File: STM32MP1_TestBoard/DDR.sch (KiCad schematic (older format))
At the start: 63 parts, among them U1 STM32MP157xAB, U2 MT41K256M16TW-107

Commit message: updated bom, readme
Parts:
- removed U1: STM32MP157xAB, STM32MP151_LFBGA:BGA-361_19x19_16.0x16.0mm, symbol STM32MP151:STM32MP151xAB
- added U1: STM32MP157xAB, STM32MP151_LFBGA:BGA-361_19x19_16.0x16.0mm, symbol STM32MP15x:STM32MP157xAB
- gave numbers to parts that had none: 55

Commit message: minor schema updates
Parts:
- added R2, R52: 1K, Resistor_SMD:R_0402_1005Metric_Pad0.72x0.64mm_HandSolder, symbol Device:R
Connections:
- wire segments 311 -> 316
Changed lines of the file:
@@
 Wire Wire Line
 	4700 5175 5325 5175
-Text HLabel 5325 5175 2    50   Input ~ 0
-DDR_VREF
 Wire Wire Line
 	1500 8650 1500 8500
@@
 	1    0    0    -1
 $EndComp
+$Comp
+L Device:R R?
+U 1 1 5FDCF44A
+P 6150 8325
+AR Path="/5FBD70AB/5FDCF44A" Ref="R?"  Part="1"
+AR Path="/60386EBB/5FDCF44A" Ref="R2"  Part="1"
+F 0 "R2" H 6220 8371 50  0000 L CNN
+F 1 "1K" H 6220 8280 50  0000 L CNN
+F 2 "Resistor_SMD:R_0402_1005Metric_Pad0.72x0.64mm_HandSolder" V 6080 8325 50  0001 C CNN
+F 3 "~" H 6150 8325 50  0001 C CNN
+F 4 "~" H 6150 8325 50  0001 C CNN "Mfr"
+F 5 "~" H 6150 8325 50  0001 C CNN "PartNo"
+	1    6150 8325
+	1    0    0    -1
+$EndComp
+$Comp
+L Device:R R?
+U 1 1 5FDCF452
+P 6150 8900
+AR Path="/5FBD70AB/5FDCF452" Ref="R?"  Part="1"
+AR Path="/60386EBB/5FDCF452" Ref="R52"  Part="1"
+F 0 "R52" H 6220 8946 50  0000 L CNN
+F 1 "1K" H 6220 8855 50  0000 L CNN
+F 2 "Resistor_SMD:R_0402_1005Metric_Pad0.72x0.64mm_HandSolder" V 6080 8900 50  0001 C CNN
+F 3 "~" H 6150 8900 50  0001 C CNN
+F 4 "~" H 6150 8900 50  0001 C CNN "Mfr"
+F 5 "~" H 6150 8900 50  0001 C CNN "PartNo"
+	1    6150 8900
+	1    0    0    -1
+$EndComp
+Wire Wire Line
+	6975 8625 6150 8625
+Wire Wire Line
+	6150 8475 6150 8625
+Connection ~ 6150 8625
+Wire Wire Line
+	6150 8625 6150 8750
+$Comp
+L power:+1V35 #PWR?
+U 1 1 5FDCF45C
+P 6150 8075
+AR Path="/5FDCF45C" Ref="#PWR?"  Part="1"
+AR Path="/6044C48A/5FDCF45C" Ref="#PWR?"  Part="1"
+AR Path="/5FBD70AB/5FDCF45C" Ref="#PWR?"  Part="1"
+AR Path="/60386EBB/5FDCF45C" Ref="#PWR0127"  Part="1"
+F 0 "#PWR0127" H 6150 7925 50  0001 C CNN
+F 1 "+1V35" H 6165 8248 50  0000 C CNN
+F 2 "" H 6150 8075 50  0001 C CNN
+F 3 "" H 6150 8075 50  0001 C CNN
+	1    6150 8075
+	1    0    0    -1
+$EndComp
+Wire Wire Line
+	6150 8075 6150 8175
+$Comp
+L power:GNDS #PWR?
+U 1 1 5FDCF463
+P 6150 9150
+AR Path="/5FBD70AB/5FDCF463" Ref="#PWR?"  Part="1"
+AR Path="/60386EBB/5FDCF463" Ref="#PWR0134"  Part="1"
+F 0 "#PWR0134" H 6150 8900 50  0001 C CNN
+F 1 "GNDS" H 6155 8977 50  0000 C CNN
+F 2 "" H 6150 9150 50  0001 C CNN
+F 3 "" H 6150 9150 50  0001 C CNN
+	1    6150 9150
+	1    0    0    -1
+$EndComp
+Wire Wire Line
+	6150 9150 6150 9050
+Text Label 5325 5175 2    50   ~ 0
+DDR_VREF
+Text Label 6975 8625 2    50   ~ 0
+DDR_VREF
 $EndSCHEMATC

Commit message: updated schematic design
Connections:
- net labels added: 1.35V_VDDQ_DDR
- net labels removed: +1V35
- wire segments 316 -> 317
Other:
- moved on the sheet: C40, C41, C42, C43, C44, C45, C46, C47, C48, C49, C50, C51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

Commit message: layout update
backup. work in progress
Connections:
- net DDR_CLKN renamed DDR_CLK_N
- net DDR_CLKP renamed DDR_CLK_P
- net DDR_DQS0N renamed DDR_DQS0_N
- net DDR_DQS0P renamed DDR_DQS0_P
- net DDR_DQS1N renamed DDR_DQS1_N
- net DDR_DQS1P renamed DDR_DQS1_P
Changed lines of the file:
@@
 	8375 5125 9350 5125
 Text Label 1950 3325 0    50   ~ 0
-DDR_DQS0P
+DDR_DQS0_P
 Text Label 9350 5025 2    50   ~ 0
-DDR_DQS0P
+DDR_DQS0_P
 Text Label 9350 5125 2    50   ~ 0
-DDR_DQS0N
+DDR_DQS0_N
 Text Label 1950 3425 0    50   ~ 0
-DDR_DQS0N
+DDR_DQS0_N
 Wire Wire Line
 	1950 4625 2900 4625
@@
 	1950 5575 2900 5575
 Text Label 1950 4525 0    50   ~ 0
-DDR_DQS1P
+DDR_DQS1_P
 Text Label 1950 4625 0    50   ~ 0
-DDR_DQS1N
+DDR_DQS1_N
 Text Label 9350 4825 2    50   ~ 0
-DDR_DQS1P
+DDR_DQS1_P
 Text Label 9350 4925 2    50   ~ 0
-DDR_DQS1N
+DDR_DQS1_N
 Text Label 1950 3525 0    50   ~ 0
 DDR_DQM0
@@
 Wire Wire Line
 	6975 5025 6350 5025
-Text Label 6350 4825 0    50   ~ 0
-DDR_CLKP
-Text Label 6350 4925 0    50   ~ 0
-DDR_CLKN
 Text Label 6350 5025 0    50   ~ 0
 DDR_CKE
@@
 	4700 2625 5325 2625
 Text Label 5325 2525 2    50   ~ 0
-DDR_CLKP
+DDR_CLK_P
 Text Label 5325 2625 2    50   ~ 0
-DDR_CLKN
+DDR_CLK_N
 Wire Wire Line
 	8375 5325 8750 5325
@@
 	4450 8050 3825 8050
 Text Label 5375 8050 2    50   ~ 0
-DDR_CLKP
+DDR_CLK_P
 Text Label 3825 8050 0    50   ~ 0
-DDR_CLKN
+DDR_CLK_N
 $Comp
 L Device:R R14
@@
 Wire Wire Line
 	5075 9550 5275 9550
+Text Label 6350 4925 0    50   ~ 0
+DDR_CLK_N
+Text Label 6350 4825 0    50   ~ 0
+DDR_CLK_P
 $EndSCHEMATC

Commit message: updated to use stm32MP15x symbol library
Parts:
- U1: Mfr STMicroelectronics -> (none); PartNo STM32MP157FAB -> (none)
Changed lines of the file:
@@
 0.5 × VDD
-$Comp
-L STM32MP15x:STM32MP157xAB U1
-U 3 1 601FCD98
-P 3800 4125
-F 0 "U1" H 3800 5990 50  0000 C CNN
-F 1 "STM32MP157xAB" H 3800 5899 50  0000 C CNN
-F 2 "STM32MP151_LFBGA:BGA-361_19x19_16.0x16.0mm" H 3650 6025 50  0001 C CNN
-F 3 "https://www.st.com/resource/en/datasheet/stm32mp157f.pdf" H 4100 4625 50  0001 C CNN
-F 4 "STMicroelectronics" H 3800 4125 50  0001 C CNN "Mfr"
-F 5 "STM32MP157FAB" H 3800 4125 50  0001 C CNN "PartNo"
-	3    3800 4125
-	1    0    0    -1
-$EndComp
 $Comp
 L Device:R R?
@@
 Text Label 6350 4825 0    50   ~ 0
 DDR_CLK_P
+$Comp
+L STM32MP15x:STM32MP157xAB U1
+U 3 1 5FBF8FCC
+P 3800 4125
+F 0 "U1" H 3800 5990 50  0000 C CNN
+F 1 "STM32MP157xAB" H 3800 5899 50  0000 C CNN
+F 2 "STM32MP151_LFBGA:BGA-361_19x19_16.0x16.0mm" H 3650 6025 50  0001 C CNN
+F 3 "https://www.st.com/resource/en/datasheet/stm32mp151c.pdf" H 4450 4275 50  0001 C CNN
+	3    3800 4125
+	1    0    0    -1
+$EndComp
 $EndSCHEMATC

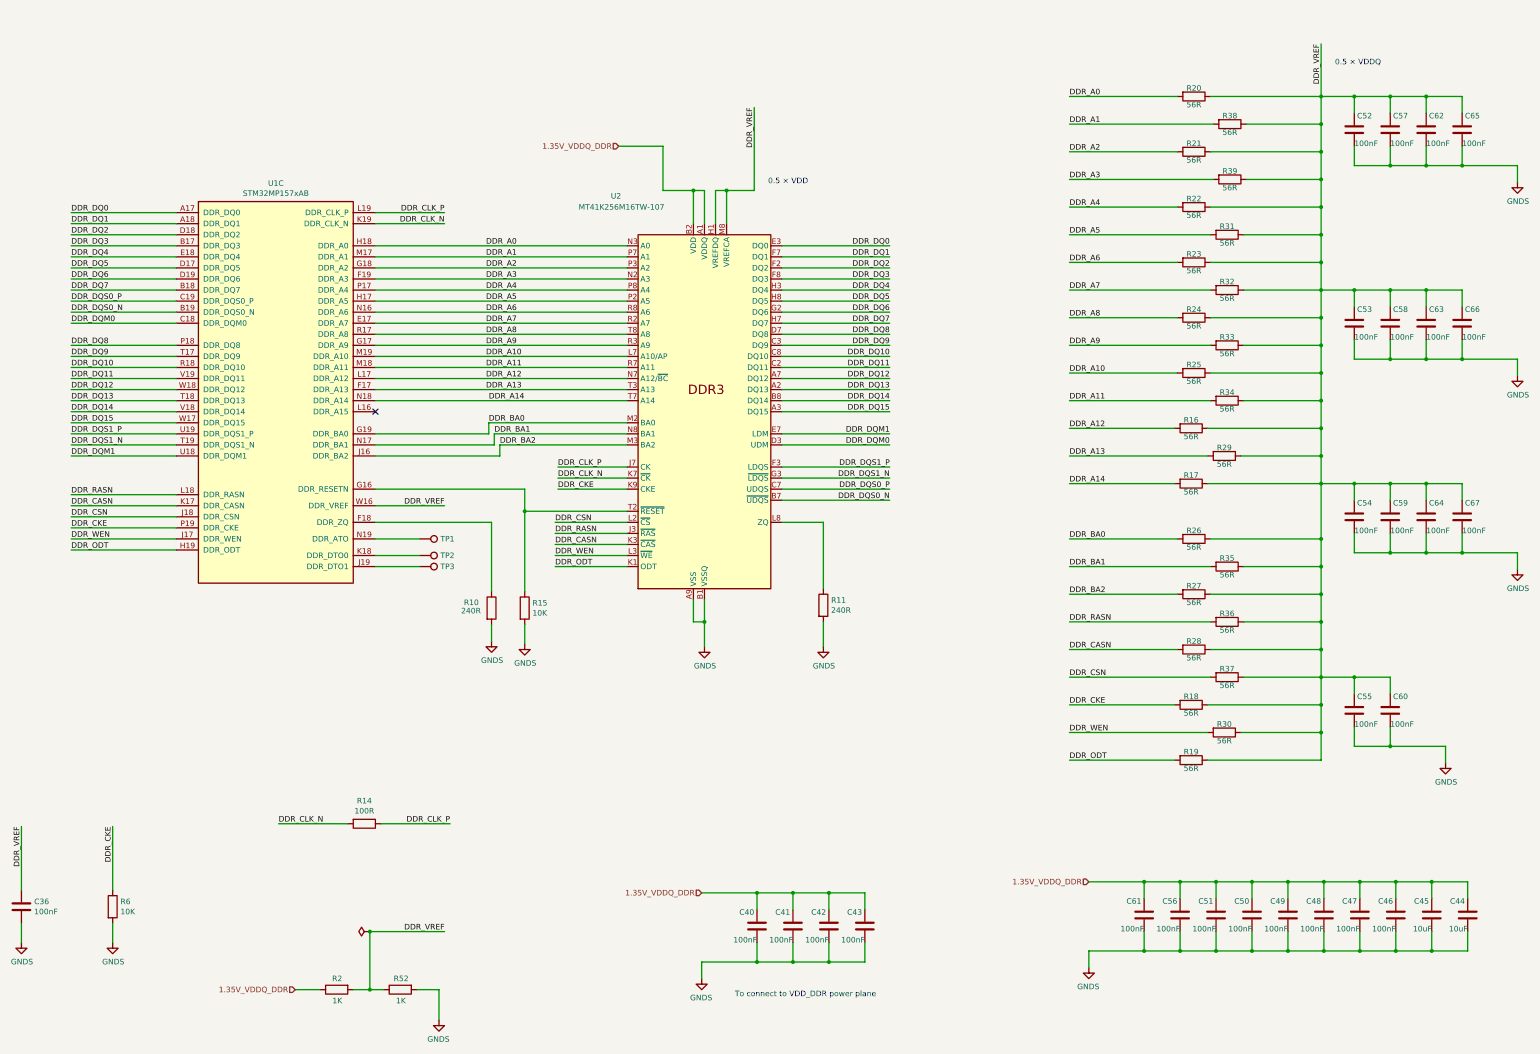
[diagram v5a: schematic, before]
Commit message: added traces for sdio, dsi and swd connectors
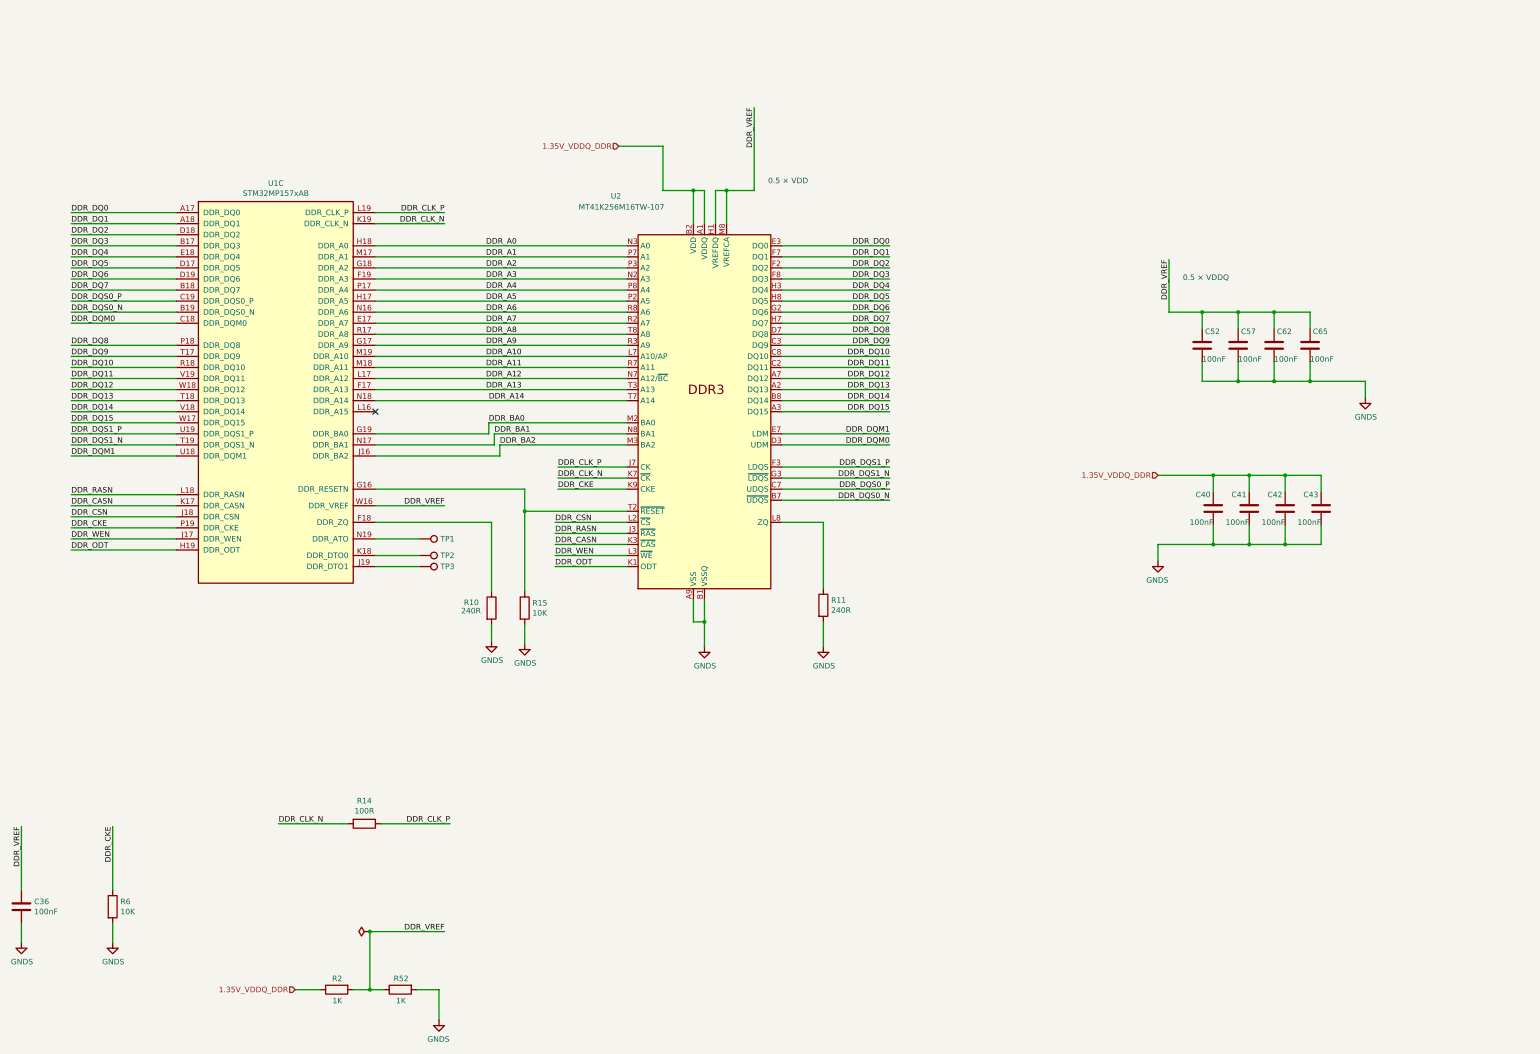
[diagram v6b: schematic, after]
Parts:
- removed C44, C45: 10uF, Capacitor_SMD:C_0402_1005Metric_Pad0.74x0.62mm_HandSolder, symbol Device:C
- removed C46, C47, C48, C49, C50, C51, C53, C54, C55, C56, C58, C59, C60, C61, C63, C64, C66, C67: 100nF, Capacitor_SMD:C_0402_1005Metric_Pad0.74x0.62mm_HandSolder, symbol Device:C
- removed R16, R17, R18, R19, R20, R21, R22, R23, R24, R25, R26, R27, R28, R29, R30, R31, R32, R33, R34, R35, R36, R37, R38, R39: 56R, Resistor_SMD:R_0402_1005Metric_Pad0.72x0.64mm_HandSolder, symbol Device:R
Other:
- note removed: "To connect to VDD_DDR power plane"
- moved on the sheet: C40, C41, C42, C43, C52, C57, C62, C65

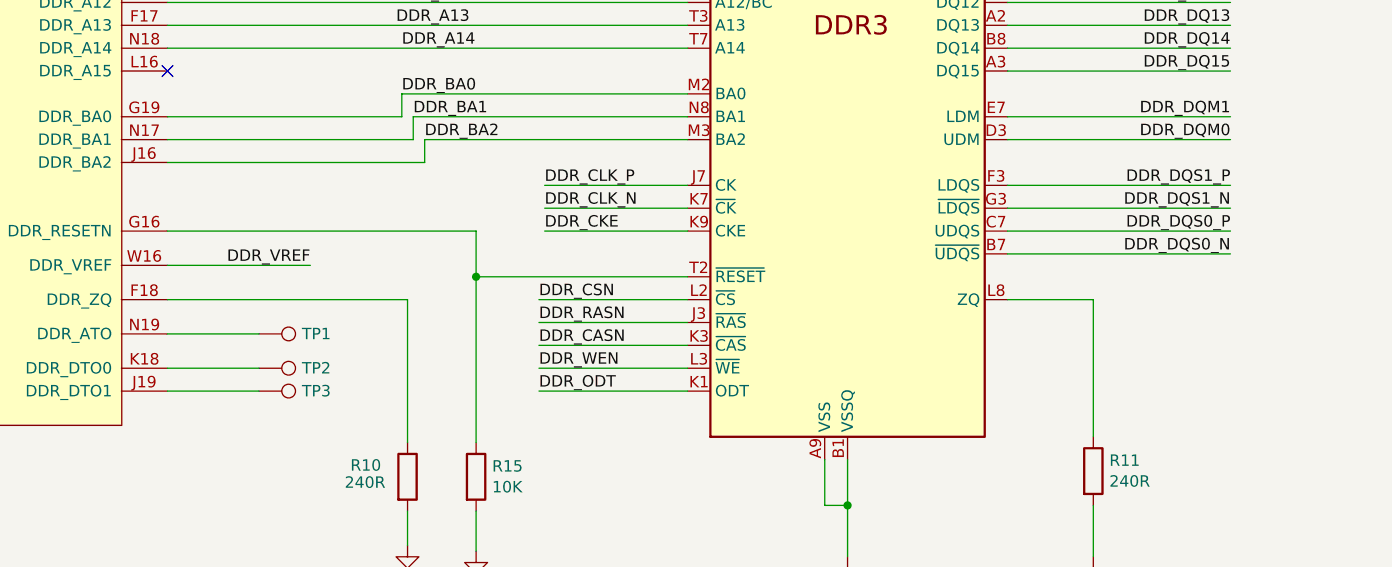
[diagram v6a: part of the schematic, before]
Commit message: swapped DDR3 high/low strobe diff pairs
- corrected DRC errors
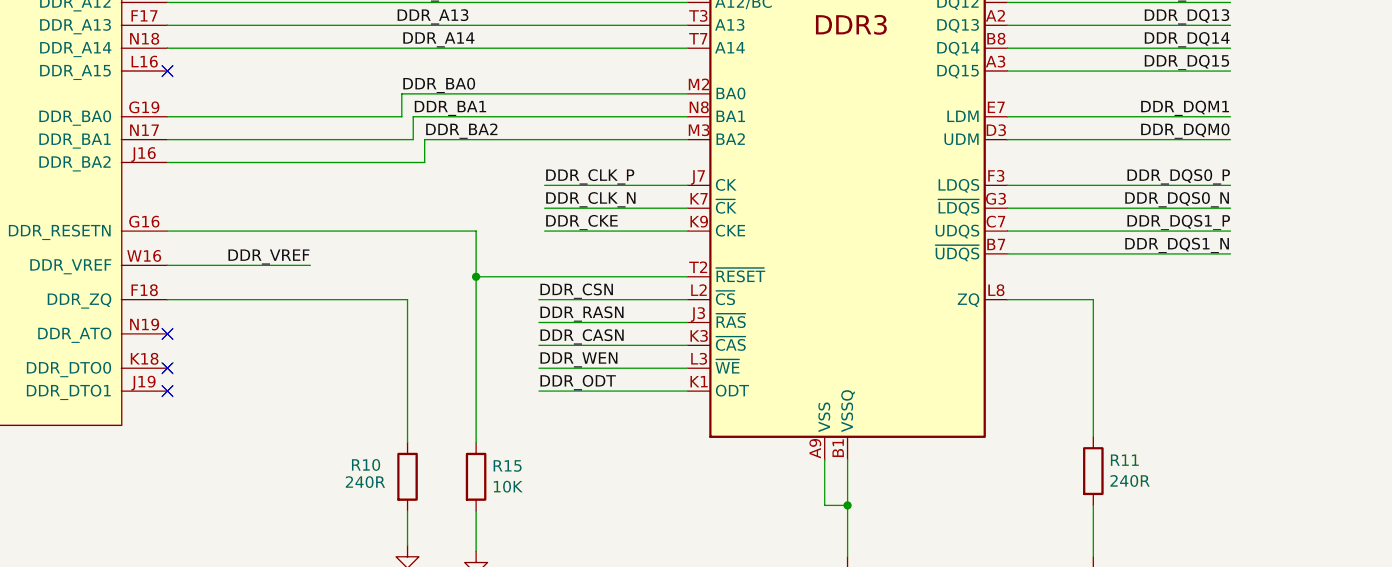
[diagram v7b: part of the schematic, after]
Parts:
- removed TP1, TP2, TP3: ~, TestPoint:TestPoint_Pad_D1.0mm, symbol Connector:TestPoint
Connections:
- net DDR_DQS0_N: now also U2.G3 (~LDQS); no longer U2.B7 (~UDQS)
- net DDR_DQS0_P: now also U2.F3 (LDQS); no longer U2.C7 (UDQS)
- net DDR_DQS1_N: now also U2.B7 (~UDQS); no longer U2.G3 (~LDQS)
- net DDR_DQS1_P: now also U2.C7 (UDQS); no longer U2.F3 (LDQS)
- no-connect marks 1 -> 4
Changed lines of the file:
@@
 	1    0    0    -1
 $EndComp
-$Comp
-L Connector:TestPoint TP1
-U 1 1 605AADE6
-P 5100 5475
-F 0 "TP1" V 5100 5663 50  0000 L CNN
-F 1 "~" V 5145 5663 50  0000 L CNN
-F 2 "TestPoint:TestPoint_Pad_D1.0mm" H 5300 5475 50  0001 C CNN
-F 3 "~" H 5300 5475 50  0001 C CNN
-F 4 "~" H 5100 5475 50  0001 C CNN "Mfr"
-F 5 "~" H 5100 5475 50  0001 C CNN "PartNo"
-	1    5100 5475
-	0    1    1    0
-$EndComp
-Wire Wire Line
-	5100 5475 4700 5475
-$Comp
-L Connector:TestPoint TP2
-U 1 1 605ACCD6
-P 5100 5625
-F 0 "TP2" V 5100 5813 50  0000 L CNN
-F 1 "~" V 5145 5813 50  0000 L CNN
-F 2 "TestPoint:TestPoint_Pad_D1.0mm" H 5300 5625 50  0001 C CNN
-F 3 "~" H 5300 5625 50  0001 C CNN
-F 4 "~" H 5100 5625 50  0001 C CNN "Mfr"
-F 5 "~" H 5100 5625 50  0001 C CNN "PartNo"
-	1    5100 5625
-	0    1    1    0
-$EndComp
-Wire Wire Line
-	5100 5625 4700 5625
-$Comp
-L Connector:TestPoint TP3
-U 1 1 605AE22F
-P 5100 5725
-F 0 "TP3" V 5100 5913 50  0000 L CNN
-F 1 "~" V 5145 5913 50  0000 L CNN
-F 2 "TestPoint:TestPoint_Pad_D1.0mm" H 5300 5725 50  0001 C CNN
-F 3 "~" H 5300 5725 50  0001 C CNN
-F 4 "~" H 5100 5725 50  0001 C CNN "Mfr"
-F 5 "~" H 5100 5725 50  0001 C CNN "PartNo"
-	1    5100 5725
-	0    1    1    0
-$EndComp
-Wire Wire Line
-	5100 5725 4700 5725
 Wire Wire Line
 	2900 2525 1950 2525
@@
 Text Label 1950 3325 0    50   ~ 0
 DDR_DQS0_P
-Text Label 9350 5025 2    50   ~ 0
+Text Label 9350 4825 2    50   ~ 0
 DDR_DQS0_P
-Text Label 9350 5125 2    50   ~ 0
+Text Label 9350 4925 2    50   ~ 0
 DDR_DQS0_N
 Text Label 1950 3425 0    50   ~ 0
@@
 Text Label 1950 4625 0    50   ~ 0
 DDR_DQS1_N
-Text Label 9350 4825 2    50   ~ 0
+Text Label 9350 5025 2    50   ~ 0
 DDR_DQS1_P
-Text Label 9350 4925 2    50   ~ 0
+Text Label 9350 5125 2    50   ~ 0
 DDR_DQS1_N
 Text Label 1950 3525 0    50   ~ 0
@@
 	1    0    0    -1
 $EndComp
+NoConn ~ 4700 5475
+NoConn ~ 4700 5625
+NoConn ~ 4700 5725
 $EndSCHEMATC

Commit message: updated schema and bom docs
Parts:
- U1: value STM32MP157xAB -> STM32MP157xAC
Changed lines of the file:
@@
 F 2 "Capacitor_SMD:C_0402_1005Metric_Pad0.74x0.62mm_HandSolder" H 1538 8650 50  0001 C CNN
 F 3 "~" H 1500 8800 50  0001 C CNN
+F 4 "~" H 1500 8800 50  0001 C CNN "Mfr"
+F 5 "~" H 1500 8800 50  0001 C CNN "PartNo"
 	1    1500 8800
 	1    0    0    -1
@@
 F 2 "Capacitor_SMD:C_0402_1005Metric_Pad0.74x0.62mm_HandSolder" H 12213 3575 50  0001 C CNN
 F 3 "~" H 12175 3725 50  0001 C CNN
+F 4 "~" H 12175 3725 50  0001 C CNN "Mfr"
+F 5 "~" H 12175 3725 50  0001 C CNN "PartNo"
 	1    12175 3725
 	1    0    0    -1
@@
 F 2 "Capacitor_SMD:C_0402_1005Metric_Pad0.74x0.62mm_HandSolder" H 12538 3575 50  0001 C CNN
 F 3 "~" H 12500 3725 50  0001 C CNN
+F 4 "~" H 12500 3725 50  0001 C CNN "Mfr"
+F 5 "~" H 12500 3725 50  0001 C CNN "PartNo"
 	1    12500 3725
 	1    0    0    -1
@@
 F 2 "Capacitor_SMD:C_0402_1005Metric_Pad0.74x0.62mm_HandSolder" H 12863 3575 50  0001 C CNN
 F 3 "~" H 12825 3725 50  0001 C CNN
+F 4 "~" H 12825 3725 50  0001 C CNN "Mfr"
+F 5 "~" H 12825 3725 50  0001 C CNN "PartNo"
 	1    12825 3725
 	1    0    0    -1
@@
 F 2 "Capacitor_SMD:C_0402_1005Metric_Pad0.74x0.62mm_HandSolder" H 13188 3575 50  0001 C CNN
 F 3 "~" H 13150 3725 50  0001 C CNN
+F 4 "~" H 13150 3725 50  0001 C CNN "Mfr"
+F 5 "~" H 13150 3725 50  0001 C CNN "PartNo"
 	1    13150 3725
 	1    0    0    -1
@@
 F 2 "Capacitor_SMD:C_0402_1005Metric_Pad0.74x0.62mm_HandSolder" H 13288 5050 50  0001 C CNN
 F 3 "~" H 13250 5200 50  0001 C CNN
+F 4 "~" H 13250 5200 50  0001 C CNN "Mfr"
+F 5 "~" H 13250 5200 50  0001 C CNN "PartNo"
 	1    13250 5200
 	-1   0    0    -1
@@
 F 2 "Capacitor_SMD:C_0402_1005Metric_Pad0.74x0.62mm_HandSolder" H 12963 5050 50  0001 C CNN
 F 3 "~" H 12925 5200 50  0001 C CNN
+F 4 "~" H 12925 5200 50  0001 C CNN "Mfr"
+F 5 "~" H 12925 5200 50  0001 C CNN "PartNo"
 	1    12925 5200
 	-1   0    0    -1
@@
 F 2 "Capacitor_SMD:C_0402_1005Metric_Pad0.74x0.62mm_HandSolder" H 12638 5050 50  0001 C CNN
 F 3 "~" H 12600 5200 50  0001 C CNN
+F 4 "~" H 12600 5200 50  0001 C CNN "Mfr"
+F 5 "~" H 12600 5200 50  0001 C CNN "PartNo"
 	1    12600 5200
 	-1   0    0    -1
@@
 F 2 "Capacitor_SMD:C_0402_1005Metric_Pad0.74x0.62mm_HandSolder" H 12313 5050 50  0001 C CNN
 F 3 "~" H 12275 5200 50  0001 C CNN
+F 4 "~" H 12275 5200 50  0001 C CNN "Mfr"
+F 5 "~" H 12275 5200 50  0001 C CNN "PartNo"
 	1    12275 5200
 	-1   0    0    -1
@@
 P 3800 4125
 F 0 "U1" H 3800 5990 50  0000 C CNN
-F 1 "STM32MP157xAB" H 3800 5899 50  0000 C CNN
+F 1 "STM32MP157xAC" H 3800 5899 50  0000 C CNN
 F 2 "STM32MP151_LFBGA:BGA-361_19x19_16.0x16.0mm" H 3650 6025 50  0001 C CNN
 F 3 "https://www.st.com/resource/en/datasheet/stm32mp151c.pdf" H 4450 4275 50  0001 C CNN
+F 4 "~" H 3800 4125 50  0001 C CNN "Mfr"
+F 5 "~" H 3800 4125 50  0001 C CNN "PartNo"
 	3    3800 4125
 	1    0    0    -1
